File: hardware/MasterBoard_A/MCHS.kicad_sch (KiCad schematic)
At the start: 27 parts, among them Q5 MMBT5550L, U14 DMN62D0U, U26 NCV68061, U27 MCP1501-40xSN, U28 MCP33151, U29 DMN62D0U, U33 NSI45015, U35 NSI45015, U47 MIC7300M5, U48 TLV713185PDBV, U50 MCP33151

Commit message: mb v1.1 on da way
shuffled around stuff. review notes. made notes. glory to those who look forward and all that fuzz
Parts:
- R53: value 226 -> 121; mouser https://www.mouser.com/ProductDetail/KOA-Speer/RK73H2BTTD22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 -> https://www.mouser.com/ProductDetail/SEI-Stackpole/RNCP0805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; specs 226Ohm, 250mW, 1%, 200V, -55C, +155C -> 121Ohm, 200V, 250mW, 1%, 100ppm, -55C, +155C; unit x10 0.023 -> 0.012
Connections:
- net percise_sense: now also R53.1; no longer R53.2
- net at C52.1, U28.3 (Ain+): now also R53.2; no longer R53.1
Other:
- company: (none) -> UTA Racing
- title: DHAB S124 sensor interface , SPI -> BeeMS Master Board (A)
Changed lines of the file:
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@@
 	(paper "A4")
 	(title_block
-		(title "DHAB S124 sensor interface , SPI")
+		(title "BeeMS Master Board (A)")
 		(rev "1.0")
-		(comment 1 "for use with the DHAB S124 current sensor")
+		(company "UTA Racing")
+		(comment 1 "Files at github.com/Gregification/BeeMS")
 	)
 	(text "a lot of hassle for this but it protects the bajillion dollar sensor"
@@
 	)
 	(symbol
+		(lib_id "Device:R_Small_US")
+		(at 113.03 57.15 270)
+		(mirror x)
+		(unit 1)
+		(exclude_from_sim no)
+		(in_bom yes)
+		(on_board yes)
+		(dnp no)
+		(property "Reference" "R53"
+			(at 110.617 52.197 90)
+			(effects
+				(font
+					(size 1.27 1.27)
+				)
+				(justify left)
+			)
+		)
+		(property "Value" "121"
+			(at 110.617 54.737 90)
+			(effects
+				(font
+					(size 1.27 1.27)
+				)
+				(justify left)
+			)
+		)
+		(property "Footprint" "Resistor_SMD:R_0805_2012Metric_Pad1.20x1.40mm_HandSolder"
+			(at 113.03 57.15 0)
+			(effects
+				(font
+					(size 1.27 1.27)
+				)
+				(hide yes)
+			)
+		)
+		(property "Datasheet" ""
+			(at 113.03 57.15 0)
+			(effects
+				(font
+					(size 1.27 1.27)
+				)
+				(hide yes)
+			)
+		)
+		(property "Description" "Resistor, US symbol"
+			(at 113.03 57.15 0)
+			(effects
+				(font
+					(size 1.27 1.27)
+				)
+				(hide yes)
+			)
+		)
+		(property "Sim.Device" ""
+			(at 113.03 57.15 0)
+			(effects
+				(font
+					(size 1.27 1.27)
+				)
+				(hide yes)
+			)
+		)
+		(property "Sim.Type" ""
+			(at 113.03 57.15 0)
+			(effects
+				(font
+					(size 1.27 1.27)
+				)
+				(hide yes)
+			)
+		)
+		(property "mouser" "https://www.mouser.com/ProductDetail/SEI-Stackpole/RNCP0805FTD121R?qs=sGAEpiMZZMvdGkrng054tyMPH50YnZ95dJmxWK8e%2FBgSyeAIVnAHjA%3D%3D"
+			(at 113.03 57.15 0)
+			(effects
+				(font
+					(size 1.27 1.27)
+				)
+				(hide yes)
+			)
+		)
+		(property "specs" "121Ohm, 200V, 250mW, 1%, 100ppm, -55C, +155C"
+			(at 113.03 57.15 0)
+			(effects
+				(font
+					(size 1.27 1.27)
+				)
+				(hide yes)
+			)
+		)
+		(property "unit x1" "0.10"
+			(at 113.03 57.15 0)
+			(effects
+				(font
+					(size 1.27 1.27)
+				)
+				(hide yes)
+			)
+		)
+		(property "unit x10" "0.012"
+			(at 113.03 57.15 0)
+			(effects
+				(font
+					(size 1.27 1.27)
+				)
+				(hide yes)
+			)
+		)
+		(property "Sim.Pins" ""
+			(at 113.03 57.15 90)
+			(effects
+				(font
+					(size 1.27 1.27)
+				)
+				(hide yes)
+			)
+		)
+		(property "note" ""
+			(at 113.03 57.15 90)
+			(effects
+				(font
+					(size 1.27 1.27)
+				)
+				(hide yes)
+			)
+		)
+		(pin "2"
+		)
+		(pin "1"
+		)
+		(instances
+			(project "MasterBoard_A"
+				(path "/20ac6af0-79b5-4ba6-aad3-75081d02c913/d0eed94f-9d43-4b87-adab-de47b85cc6fc"
+					(reference "R53")
+					(unit 1)
+				)
+			)
+		)
+	)
+	(symbol
 		(lib_id "zzLocalLibrary:MCP33151/41")
 		(at 83.82 78.74 0)
@@
 					(unit 1)
 				)
-			)
-		)
-	)
-	(symbol
-		(lib_id "Device:R_Small_US")
-		(at 113.03 57.15 90)
-		(unit 1)
-		(exclude_from_sim no)
-		(in_bom yes)
-		(on_board yes)
-		(dnp no)
-		(property "Reference" "R53"
-			(at 114.808 52.324 90)
-			(effects
-				(font
-					(size 1.27 1.27)
-				)
-				(justify left)
-			)
-		)
-		(property "Value" "226"
-			(at 114.808 54.864 90)
-			(effects
-				(font
-					(size 1.27 1.27)
-				)
-				(justify left)
-			)
-		)
-		(property "Footprint" "Resistor_SMD:R_0805_2012Metric_Pad1.20x1.40mm_HandSolder"
-			(at 113.03 57.15 0)
-			(effects
-				(font
-					(size 1.27 1.27)
-				)
-				(hide yes)
-			)
-		)
-		(property "Datasheet" ""
-			(at 113.03 57.15 0)
-			(effects
-				(font
-					(size 1.27 1.27)
-				)
-				(hide yes)
-			)
-		)
-		(property "Description" "Resistor, US symbol"
-			(at 113.03 57.15 0)
-			(effects
-				(font
-					(size 1.27 1.27)
-				)
-				(hide yes)
-			)
-		)
-		(property "Sim.Device" ""
-			(at 113.03 57.15 0)
-			(effects
-				(font
-					(size 1.27 1.27)
-				)
-				(hide yes)
-			)
-		)
-		(property "Sim.Type" ""
-			(at 113.03 57.15 0)
-			(effects
-				(font
-					(size 1.27 1.27)
-				)
-				(hide yes)
-			)
-		)
-		(property "mouser" "https://www.mouser.com/ProductDetail/KOA-Speer/RK73H2BTTD2260F?qs=sGAEpiMZZMvdGkrng054t0wRT%252B902PGcT6B0yBPcmBs%3D"
-			(at 113.03 57.15 0)
-			(effects
-				(font
-					(size 1.27 1.27)
-				)
-				(hide yes)
-			)
-		)
-		(property "specs" "226Ohm, 250mW, 1%, 200V, -55C, +155C"
-			(at 113.03 57.15 0)
-			(effects
-				(font
-					(size 1.27 1.27)
-				)
-				(hide yes)
-			)
-		)
-		(property "unit x1" "0.10"
-			(at 113.03 57.15 0)
-			(effects
-				(font
-					(size 1.27 1.27)
-				)
-				(hide yes)
-			)
-		)
-		(property "unit x10" "0.023"
-			(at 113.03 57.15 0)
-			(effects
-				(font
-					(size 1.27 1.27)
-				)
-				(hide yes)
-			)
-		)
-		(property "Sim.Pins" ""
-			(at 113.03 57.15 90)
-			(effects
-				(font
-					(size 1.27 1.27)
-				)
-				(hide yes)
-			)
-		)
-		(property "note" ""
-			(at 113.03 57.15 90)
-			(effects
-				(font
-					(size 1.27 1.27)
-				)
-				(hide yes)
-			)
-		)
-		(pin "2"
-		)
-		(pin "1"
-		)
-		(instances
-			(project "MasterBoard_A"
-				(path "/20ac6af0-79b5-4ba6-aad3-75081d02c913/d0eed94f-9d43-4b87-adab-de47b85cc6fc"
-					(reference "R53")
-					(unit 1)
-				)

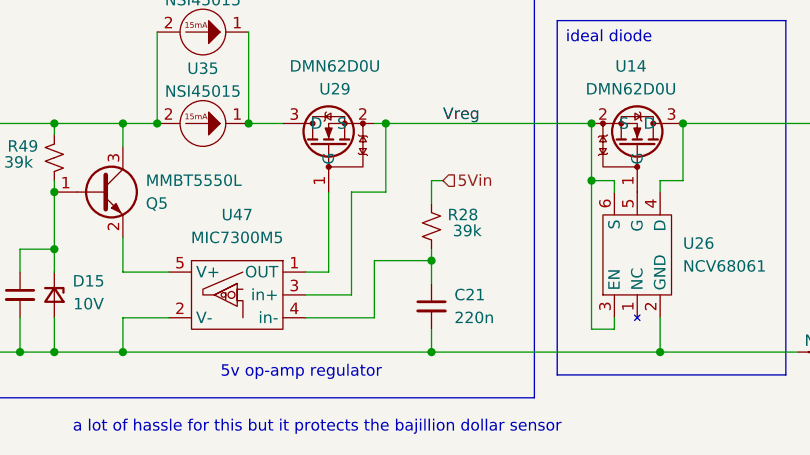
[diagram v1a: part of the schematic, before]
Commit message: buhhhh
the wizzard is back. help. decimated the totem pole optocoupler symbol , some pins were where they werent supposed to be
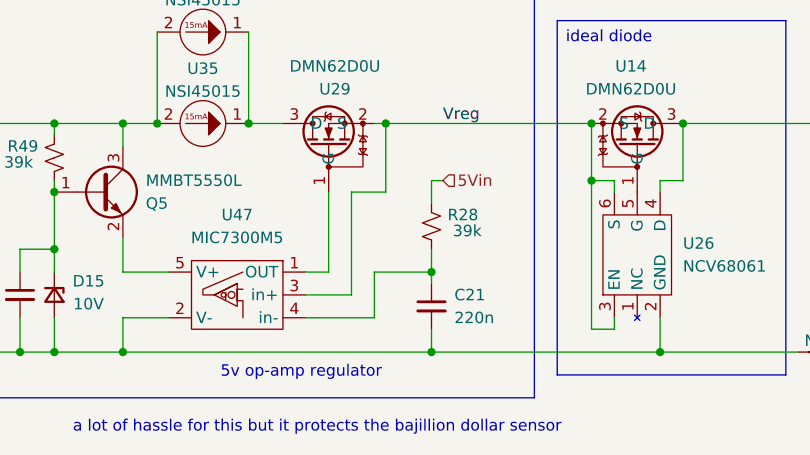
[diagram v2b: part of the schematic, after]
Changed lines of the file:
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@@
+	)
+	(junction
+		(at 87.63 140.97)
+		(diameter 0)
+		(color 0 0 0 0)
 	)
 	(junction
@@
 	)
 	(junction
-		(at 87.63 139.7)
-		(diameter 0)
-		(color 0 0 0 0)
-	)
-	(junction
 		(at 68.58 20.32)
 		(diameter 0)
@@
 	(wire
 		(pts
-			(xy 87.63 139.7) (xy 87.63 142.24)
-		)
-		(stroke
-			(width 0)
-			(type default)
-		)
-	)
-	(wire
-		(pts
 			(xy 45.72 124.46) (xy 53.34 124.46)
 		)
@@
 	(wire
 		(pts
+			(xy 87.63 140.97) (xy 87.63 142.24)
+		)
+		(stroke
+			(width 0)
+			(type default)
+		)
+	)
+	(wire
+		(pts
 			(xy 129.54 17.78) (xy 140.97 17.78)
 		)
@@
 	(wire
 		(pts
-			(xy 87.63 138.43) (xy 87.63 139.7)
+			(xy 87.63 138.43) (xy 87.63 140.97)
 		)
 		(stroke
@@
 	(wire
 		(pts
-			(xy 81.28 139.7) (xy 81.28 146.05)
+			(xy 81.28 140.97) (xy 81.28 146.05)
 		)
 		(stroke
@@
 	(wire
 		(pts
-			(xy 81.28 139.7) (xy 87.63 139.7)
-		)
-		(stroke
+			(xy 81.28 140.97) (xy 87.63 140.97)
+		)
+		(stroke

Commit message: mb 1.1 on da way. more shuffling
trying to be more professional about the part choices. obtuse excel sheet of pain has arrived.
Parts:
- removed C19, C25: 10u, Capacitor_SMD:C_1206_3216Metric_Pad1.33x1.80mm_HandSolder, symbol Device:C_Small
- removed C20, C23, C4, C52, C73: 220n, Capacitor_SMD:C_0805_2012Metric_Pad1.18x1.45mm_HandSolder, symbol Device:C_Small
- removed NT3: NetTie_2, NetTie:NetTie-2_SMD_Pad2.0mm, symbol Device:NetTie_2
- removed R28, R49: 39k, Resistor_SMD:R_0805_2012Metric_Pad1.20x1.40mm_HandSolder, symbol Device:R_Small_US
- removed R52, R53: 121, Resistor_SMD:R_0805_2012Metric_Pad1.20x1.40mm_HandSolder, symbol Device:R_Small_US
- removed U14, U29: DMN62D0U, Package_TO_SOT_SMD:SOT-23_Handsoldering, symbol zzLocalLibrary:DMN62D0U
- removed U33, U35: NSI45015, Diode_SMD:D_SOD-123, symbol zzLocalLibrary:NSI45015
- added C401, C403, C405, C406, C407, C408, C409: 220n, Capacitor_SMD:C_0805_2012Metric_Pad1.18x1.45mm_HandSolder, symbol Device:C_Small
- added C404: 10n, Capacitor_SMD:C_0805_2012Metric_Pad1.18x1.45mm_HandSolder, symbol Device:C_Small
- added R402, R403: 100, Resistor_SMD:R_1206_3216Metric_Pad1.30x1.75mm_HandSolder, symbol Device:R_Small_US
- added R404, R405: 40.2k, Resistor_SMD:R_0805_2012Metric_Pad1.20x1.40mm_HandSolder, symbol Device:R_Small_US
- added U405, U406: Si1450DH, Package_TO_SOT_SMD:SOT-363_SC-70-6_Handsoldering, symbol zzLocalLibrary:Si1480DH
- added U407: NSI5030, Diode_SMD:Nexperia_CFP3_SOD-123W, symbol zzLocalLibrary:NSI45030
- renumbered C24 to C402, C21 to C410, D15 to D401, Q5 to Q401, R51 to R401, U48 to U401, U27 to U402, U28 to U403, U50 to U404, U26 to U408, U47 to U409
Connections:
- net GND_out is gone; now on net GND: U403.4 (Ain-), U404.4 (Ain-)
- net (8, 45)Vin: now also R404.2, U407.2
- net 5V_out: now also U406.1 (D), U406.2 (D), U406.5 (D), U406.6 (D)
- net 5Vin: now also C401.1, C403.1, R405.2
- net GND: now also C401.2, C403.2, C404.2, C405.2, C406.2, C407.2, C408.2, C409.2
- net Vio: now also C406.1, C407.1
- net Vreg: now also C409.1, U405.4 (S), U406.4 (S)
- net impercise_sense: now also R402.1
- net percise_sense: now also R403.1
- net 4.096Vref: now reaches U402.7 (OUT), U402.8 (FB), U403.1 (Vref), U404.1 (Vref)
- net 4.096Vref: now also C404.1
- net at U409.1 (OUT): now also U405.3 (G)
- net at C410.1, U409.4 (in-): now also R405.1
- net at D401.1 (K), Q401.1 (B): now also R404.1
- net at U408.5 (G): now also U406.3 (G)
- net at U403.3 (Ain+): now also C405.1, R403.2
- net at U404.3 (Ain+): now also C408.1, R402.2
- new net: U405.1 (D), U405.2 (D), U405.5 (D), U405.6 (D), U407.1
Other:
- moved on the sheet: C402, C410, D401, Q401, R401, U401, U402, U403, U404, U408, U409

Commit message: excel monkey has monkey do-ne it
eyeballed a format for the psu table, it gets the point across
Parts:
- removed R401: 10k, Resistor_SMD:R_0805_2012Metric_Pad1.20x1.40mm_HandSolder, symbol Device:R_Small_US
- added R404: 14.3, Resistor_SMD:R_0805_2012Metric_Pad1.20x1.40mm_HandSolder, symbol Device:R_Small_US
- R402, R403: value 100 -> 22.1k; footprint Resistor_SMD:R_1206_3216Metric_Pad1.30x1.75mm_HandSolder -> Resistor_SMD:R_0805_2012Metric_Pad1.20x1.40mm_HandSolder; mouser https://www.mouser.com/ProductDetail/ROHM-Semiconductor/ESR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 -> https://www.mouser.com/ProductDetail/YAGEO/AC0805FR-0722K1L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; specs 100 omh, thick, anti surge, 1%, 750mW, 200V, -55C, +155C, 1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 -> 22.1kR, 1%, 125mW, 150V, 100ppm, -55C, +155C; unit x1 0.17 -> 0.10; unit x10 0.055 -> 0.011
- R405: value 40.2k -> 14.3; mouser https://www.mouser.com/ProductDetail/KOA-Speer/RK73H2ATTD40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 -> https://www.mouser.com/ProductDetail/KOA-Speer/RK73H2ATTD14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; specs 40.2k ohm, 250mW, 1%, 150V, 100ppm, -55C, +155C -> 14.3R, 250mW, 1%, 100ppm, 150V, -55C, +155C; unit x1 0.1 -> 0.10
- U406: renamed from U409; footprint Package_TO_SOT_SMD:TSOT-23-5_HandSoldering -> Package_TO_SOT_SMD:TSOT-23-5
- renumbered C403 to C402, C406 to C403, C407 to C404, C402 to C405, C404 to C406, C410 to C407, C405 to C408, C408 to C409, C409 to C410, R404 to R401, U402 to U401, U401 to U402, U407 to U403, U403 to U404, U404 to U405, U405 to U407, U406 to U408, U408 to U409
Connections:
- net 5Vin: now also R402.1, R403.2; no longer R405.2
- net impercise_sense: now also R405.1; no longer R402.1
- net percise_sense: now also R404.1; no longer R403.1
- net MCHS_shutdown_N: now reaches C407.1, U406.4 (in-)
- net MCHS_shutdown_N: now also R403.1; no longer R405.1
- net at C408.1, U404.3 (Ain+): now also R404.2; no longer R403.2
- net at U402.3 (EN): now also R402.2
- net at C409.1, U405.3 (Ain+): now also R405.2; no longer R402.2
- no-connect marks 0 -> 1

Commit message: multi channel propaganda
only bots use multi channel layouts
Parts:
- D401: footprint Diode_SMD:D_2512_6332Metric_Pad1.52x3.35mm_HandSolder -> Diode_SMD:D_0805_2012Metric_Pad1.15x1.40mm_HandSolder
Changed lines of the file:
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@@
+	)
+	(symbol
+		(lib_id "Device:D_Zener_Small")
+		(at 49.53 181.61 270)
+		(unit 1)
+		(exclude_from_sim no)
+		(in_bom yes)
+		(on_board yes)
+		(dnp no)
+		(property "Reference" "D401"
+			(at 53.34 180.086 90)
+			(effects
+				(font
+					(size 1.27 1.27)
+				)
+			)
+		)
+		(property "Value" "10V"
+			(at 53.34 182.626 90)
+			(effects
+				(font
+					(size 1.27 1.27)
+				)
+			)
+		)
+		(property "Footprint" "Diode_SMD:D_0805_2012Metric_Pad1.15x1.40mm_HandSolder"
+			(at 49.53 181.61 90)
+			(effects
+				(font
+					(size 1.27 1.27)
+				)
+				(hide yes)
+			)
+		)
+		(property "Datasheet" "~"
+			(at 49.53 181.61 90)
+			(effects
+				(font
+					(size 1.27 1.27)
+				)
+				(hide yes)
+			)
+		)
+		(property "Description" "10V, 500mW, 2%, 15 Ohms, -55C, +155C"
+			(at 49.53 181.61 0)
+			(effects
+				(font
+					(size 1.27 1.27)
+				)
+				(hide yes)
+			)
+		)
+		(property "mouser" "https://www.mouser.com/ProductDetail/Taiwan-Semiconductor/BZY55B10-RBG?qs=mAH9sUMRCtu4NcimqnPZZw%3D%3D"
+			(at 49.53 181.61 0)
+			(effects
+				(font
+					(size 1.27 1.27)
+				)
+				(hide yes)
+			)
+		)
+		(property "unit x10" "0.21"
+			(at 49.53 181.61 0)
+			(effects
+				(font
+					(size 1.27 1.27)
+				)
+				(hide yes)
+			)
+		)
+		(property "unit x1" "0.31"
+			(at 49.53 181.61 0)
+			(effects
+				(font
+					(size 1.27 1.27)
+				)
+				(hide yes)
+			)
+		)
+		(property "Sim.Pins" ""
+			(at 49.53 181.61 90)
+			(effects
+				(font
+					(size 1.27 1.27)
+				)
+				(hide yes)
+			)
+		)
+		(property "note" ""
+			(at 49.53 181.61 90)
+			(effects
+				(font
+					(size 1.27 1.27)
+				)
+				(hide yes)
+			)
+		)
+		(pin "2"
+		)
+		(pin "1"
+		)
+		(instances
+			(project "MasterBoard_A"
+				(path "/20ac6af0-79b5-4ba6-aad3-75081d02c913/d0eed94f-9d43-4b87-adab-de47b85cc6fc"
+					(reference "D401")
+					(unit 1)
+				)
+			)
+		)
 	)
 	(symbol
@@
 					(unit 1)
 				)
-			)
-		)
-	)
-	(symbol
-		(lib_id "Device:D_Zener_Small")
-		(at 49.53 181.61 270)
-		(unit 1)
-		(exclude_from_sim no)
-		(in_bom yes)
-		(on_board yes)
-		(dnp no)
-		(property "Reference" "D401"
-			(at 53.34 180.086 90)
-			(effects
-				(font
-					(size 1.27 1.27)
-				)
-			)
-		)
-		(property "Value" "10V"
-			(at 53.34 182.626 90)
-			(effects
-				(font
-					(size 1.27 1.27)
-				)
-			)
-		)
-		(property "Footprint" "Diode_SMD:D_2512_6332Metric_Pad1.52x3.35mm_HandSolder"
-			(at 49.53 181.61 90)
-			(effects
-				(font
-					(size 1.27 1.27)
-				)
-				(hide yes)
-			)
-		)
-		(property "Datasheet" "~"
-			(at 49.53 181.61 90)
-			(effects
-				(font
-					(size 1.27 1.27)
-				)
-				(hide yes)
-			)
-		)
-		(property "Description" "10V, 500mW, 2%, 15 Ohms, -55C, +155C"
-			(at 49.53 181.61 0)
-			(effects
-				(font
-					(size 1.27 1.27)
-				)
-				(hide yes)
-			)
-		)
-		(property "mouser" "https://www.mouser.com/ProductDetail/Taiwan-Semiconductor/BZY55B10-RBG?qs=mAH9sUMRCtu4NcimqnPZZw%3D%3D"
-			(at 49.53 181.61 0)
-			(effects
-				(font
-					(size 1.27 1.27)
-				)
-				(hide yes)
-			)
-		)
-		(property "unit x10" "0.21"
-			(at 49.53 181.61 0)
-			(effects
-				(font
-					(size 1.27 1.27)
-				)
-				(hide yes)
-			)
-		)
-		(property "unit x1" "0.31"
-			(at 49.53 181.61 0)
-			(effects
-				(font
-					(size 1.27 1.27)
-				)
-				(hide yes)
-			)
-		)
-		(property "Sim.Pins" ""
-			(at 49.53 181.61 90)
-			(effects
-				(font
-					(size 1.27 1.27)
-				)
-				(hide yes)
-			)
-		)
-		(property "note" ""
-			(at 49.53 181.61 90)
-			(effects
-				(font
-					(size 1.27 1.27)
-				)
-				(hide yes)
-			)
-		)
-		(pin "2"
-		)
-		(pin "1"
-		)
-		(instances
-			(project "MasterBoard_A"
-				(path "/20ac6af0-79b5-4ba6-aad3-75081d02c913/d0eed94f-9d43-4b87-adab-de47b85cc6fc"
-					(reference "D401")
-					(unit 1)
-				)

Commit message: mb layout: all but mcu bundle
thou who completes thy layout must endure excel
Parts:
- removed C405: 220n, Capacitor_SMD:C_0805_2012Metric_Pad1.18x1.45mm_HandSolder, symbol Device:C_Small
- removed R402: 22.1k, Resistor_SMD:R_0805_2012Metric_Pad1.20x1.40mm_HandSolder, symbol Device:R_Small_US
- C407, D401, Q401, R401, R403, U403, U406, U407: now not fitted; now left out of the parts list
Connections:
- net 5Vin: now also C410.1, U402.3 (EN), U408.4 (S), U409.3 (EN), U409.6 (S)
- removed net Vreg: C410.1, U406.3 (in+), U407.4 (S), U408.4 (S), U409.3 (EN), U409.6 (S)
- new net: U406.3 (in+), U407.4 (S)
- no-connect marks 1 -> 5
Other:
- note added: "made to be cap-less"
- note added: "nuh uh"

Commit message: lnlnklknnk
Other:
- note added: "add 10uF tant decoupleing"
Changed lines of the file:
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@@
+		)
+	)
+	(text "add 10uF tant decoupleing"
+		(exclude_from_sim no)
+		(at 99.568 78.994 0)
+		(effects
+			(font
+				(size 1.27 1.27)
+			)
 		)
 	)
